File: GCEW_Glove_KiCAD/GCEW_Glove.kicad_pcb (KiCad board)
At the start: 2 copper layers, 49 x 48 mm, 35 parts, among them J1 Conn_02x03_Odd_Even, J2 Flex_Sensor_Inputs, SW1 SW_SPDT, SW2 SW_Push, U1 TLV809-DBV, U2 LM3668, U3 ATMEGA328PB-AU, U4 HC-05_BluetoothModule

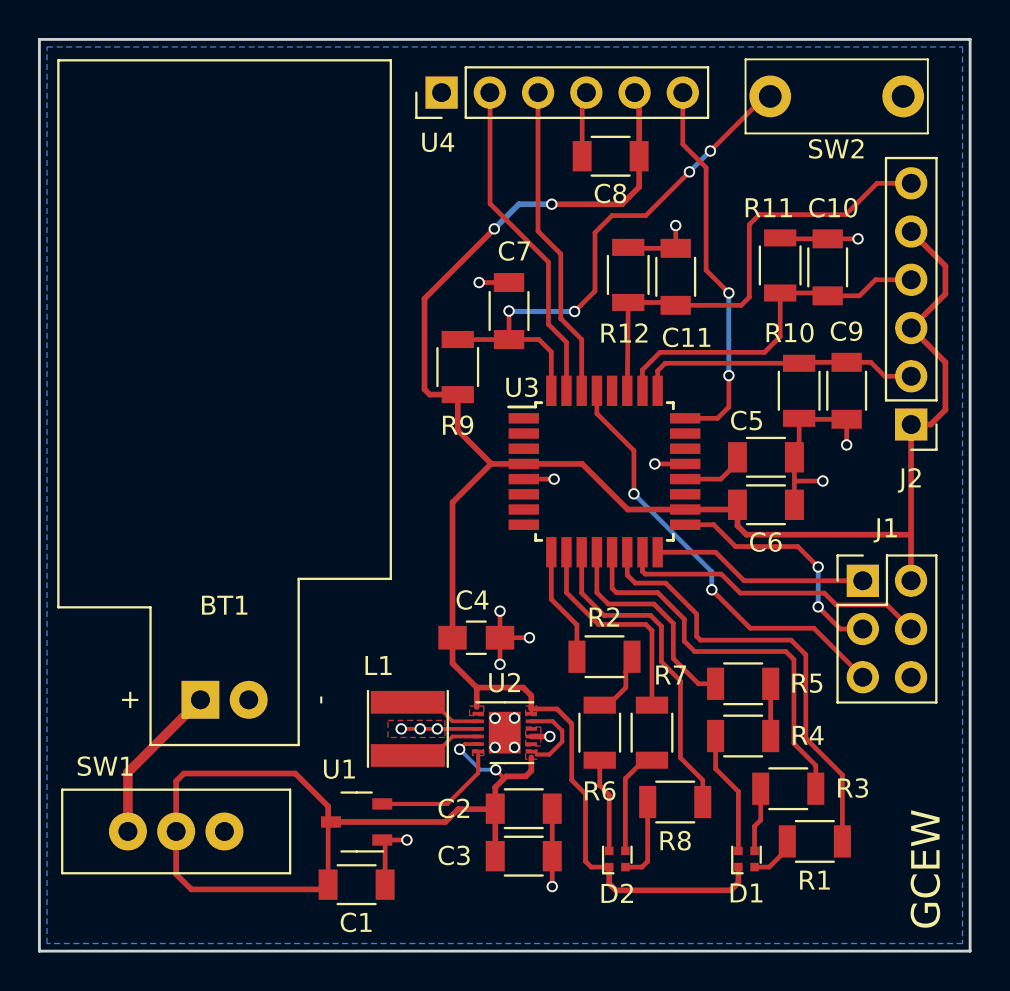
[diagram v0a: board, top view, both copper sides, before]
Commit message: GCEW Glove Schematic Update 4
Fixed PCB design error with Bluetooth module. Added additional labels on silkscreen layers.
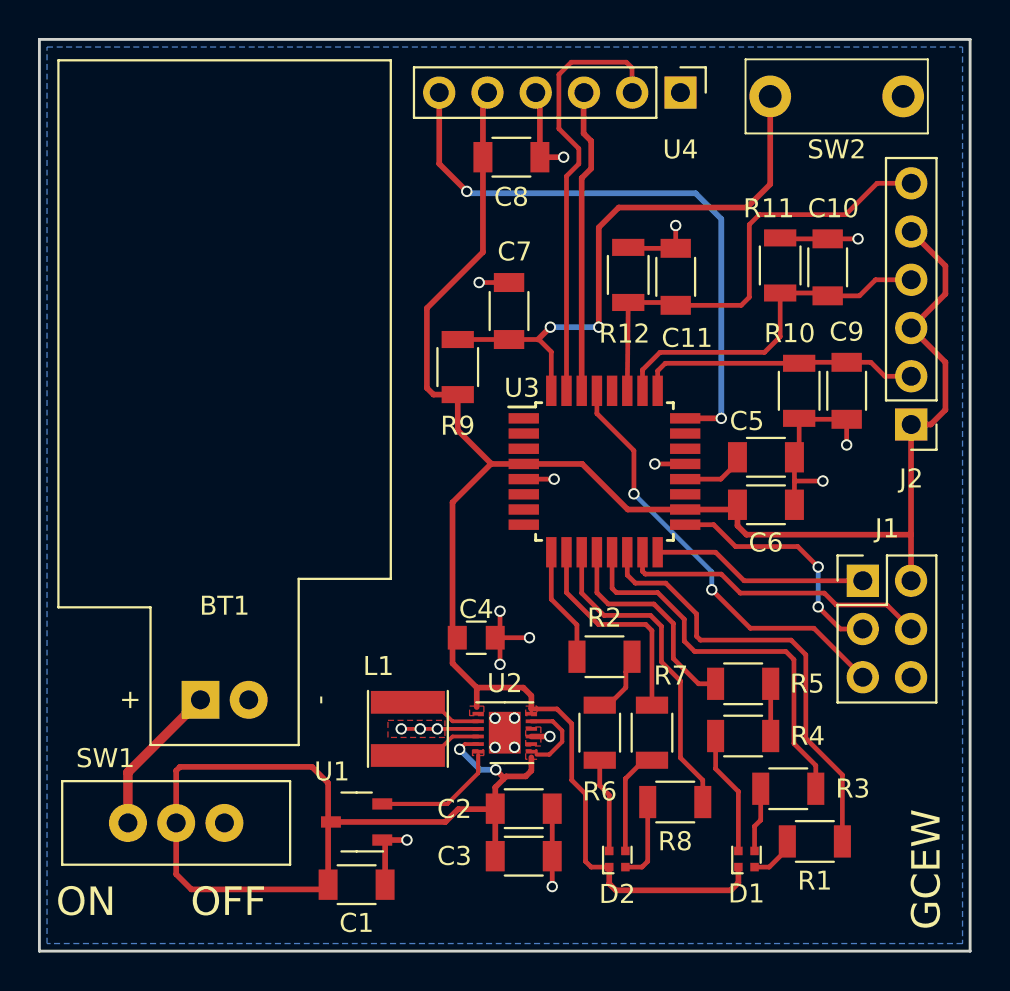
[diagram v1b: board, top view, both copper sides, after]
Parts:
- C4: footprint Capacitors_SMD:C_0805_HandSoldering -> Capacitors_SMD:C_0805
- moved U4 12.6 mm to (163.8, 102.8), turned to 270 degrees
- moved C8 5.23 mm to (154.8, 106.2), turned to 180 degrees
- moved SW1 0.45 mm to (137.2, 141.2)
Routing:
- net Net-(U3-Pad24): track 20.1 -> 32.2 mm
- net +3.3V: track 114.5 -> 107.7 mm, vias 2 -> 0
- net HC-05_RX: track 17.4 -> 22.9 mm
- net Net-(C7-Pad2): track 29.0 -> 30.7 mm, vias 4 -> 2
- net GND: track 47.0 -> 48.3 mm, vias 20 -> 21
- net VCC: track 50.9 -> 52.0 mm
- net HC-05_TX: track 16.7 -> 16.1 mm
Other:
- board text added: "F1"
- board text added: "F2"
- board text added: "F3"
- board text added: "OFF"
- board text added: "ON"
